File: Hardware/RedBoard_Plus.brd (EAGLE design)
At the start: 68.6 x 58.4 mm, 171 parts, among them IC3 LM1117, J2 ISP, J3 5.5x2.1mm Barrel, J4 QWIIC_RIGHT_ANGLE, J5 USB Female Type C Connector, Q1 20V/4.2A/52mΩ/1.4W, Q2 310mA/60V/1.6Ω, Q3 310mA/60V/1.6Ω, U3 3.3V, U4 ATMEGA328P_TQFP, U5 CH340C, Y1 16MHz

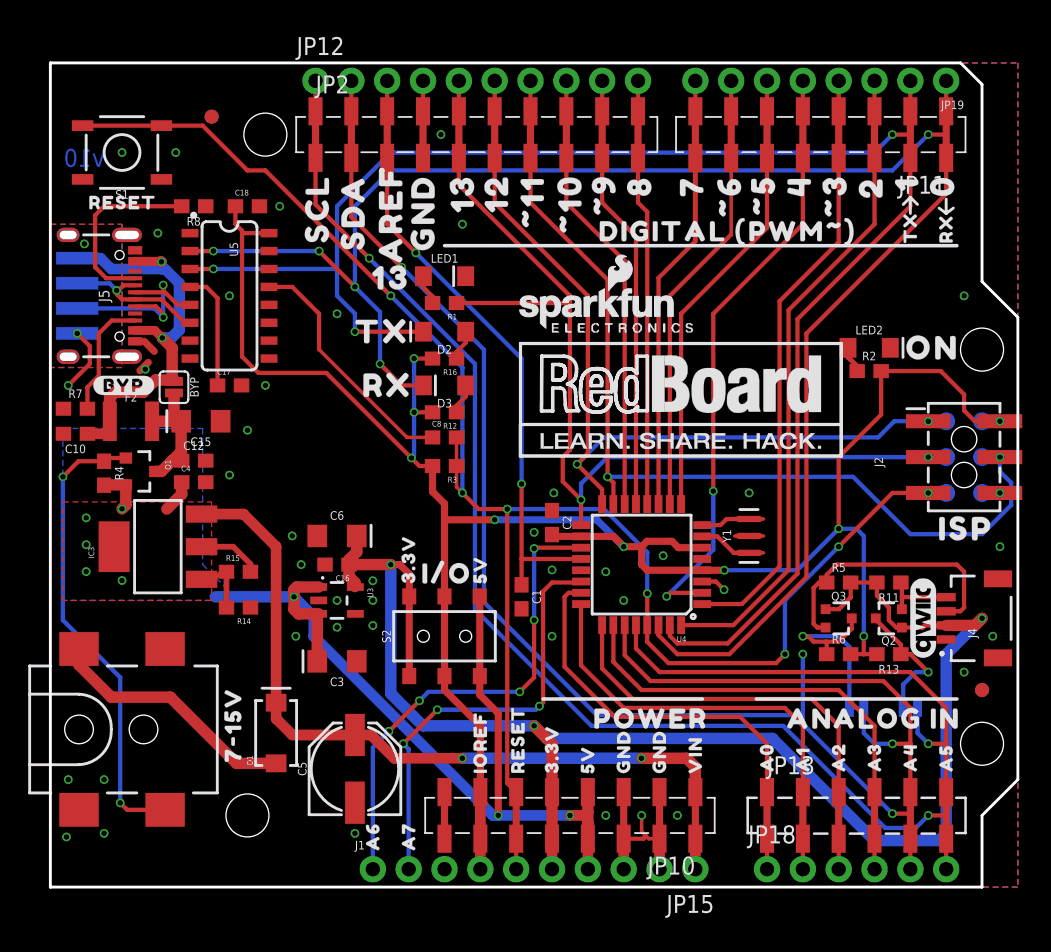
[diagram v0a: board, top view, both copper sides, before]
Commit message: Pete's design review notes:
SF logo on back
GND vias next to USB C
Remove 4-way nodes on sch
Remove overlapping text on sch
Move SFE logo in sch
Sch typo
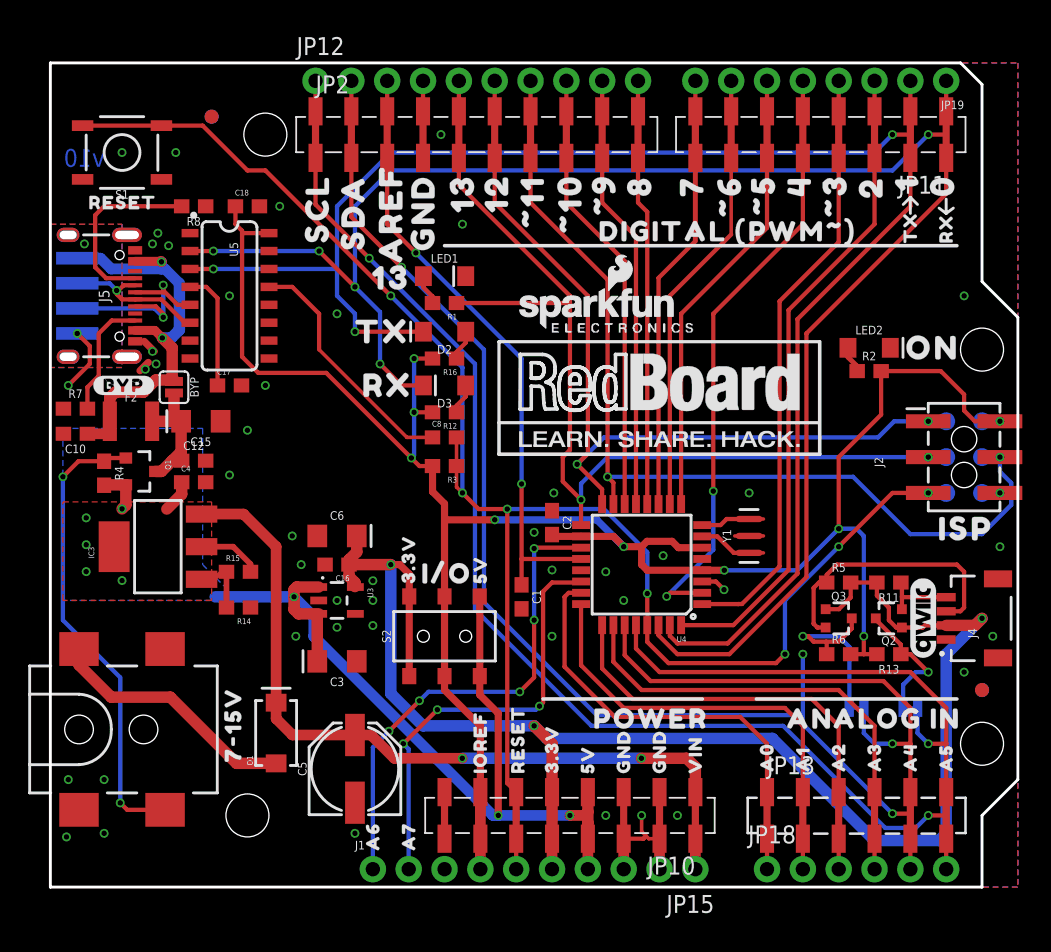
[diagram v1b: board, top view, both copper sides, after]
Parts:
- added U$101: (no value), SparkFun-Aesthetics:SFE_LOGO_FLAME_.2
- added U$3: REDBOARD_LOGO, redboard_logo:REDBOARD_LOGO
- U$78: value REDBOARD_LOGO -> (none); device redboard_logo:REDBOARD_LOGO -> SparkFun-Aesthetics:SFE_LOGO_NAME_.3
- moved U$1 33.5 mm to (31.8, 30.5), flipped to the top
- moved U$78 3.69 mm to (33.0, 26.7), flipped to the bottom
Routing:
- net GND: vias 44 -> 48
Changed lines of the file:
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@@
 <drawing>
 <settings>
-<setting alwaysvectorfont="no"/>
+<setting alwaysvectorfont="yes"/>
 <setting keepoldvectorfont="yes"/>
 <setting verticaltext="up"/>
@@
 <layers>
 <layer number="1" name="Top" color="4" fill="1" visible="yes" active="yes"/>
+<layer number="15" name="Route15" color="4" fill="6" visible="no" active="yes"/>
 <layer number="16" name="Bottom" color="1" fill="1" visible="yes" active="yes"/>
 <layer number="17" name="Pads" color="2" fill="1" visible="yes" active="yes"/>
@@
 <layer number="89" name="SimProbes" color="9" fill="1" visible="no" active="no"/>
 <layer number="90" name="Modules" color="5" fill="1" visible="no" active="no"/>
+<layer number="2" name="Route2" color="1" fill="3" visible="no" active="no"/>
 <layer number="3" name="Route3" color="4" fill="3" visible="no" active="no"/>
 <layer number="4" name="Route4" color="1" fill="4" visible="no" active="no"/>
@@
 <element name="U$100" library="output" package="_GND0" value="" x="26.416" y="43.307" smashed="yes" rot="R90"/>
 <element name="U$21" library="output" package="_GND0" value="" x="26.416" y="57.658" smashed="yes" rot="MR270"/>
-<element name="U$78" library="redboard_logo" package="REDBOARD_LOGO" value="REDBOARD_LOGO" x="33.274" y="30.353" smashed="yes"/>
-<element name="U$1" library="redboard_logo" package="REDBOARD_LOGO" value="REDBOARD_LOGO" x="62.992" y="42.672" smashed="yes" rot="MR0"/>
 <element name="FD1" library="SparkFun-Aesthetics" package="FIDUCIAL-1X2" value="FIDUCIAL1X2" x="11.43" y="54.61" smashed="yes" rot="MR0"/>
 <element name="FD2" library="SparkFun-Aesthetics" package="FIDUCIAL-1X2" value="FIDUCIAL1X2" x="66.04" y="13.97" smashed="yes" rot="MR0"/>
+<element name="U$1" library="redboard_logo" package="REDBOARD_LOGO" value="REDBOARD_LOGO" x="31.75" y="30.48" smashed="yes"/>
+<element name="U$3" library="redboard_logo" package="REDBOARD_LOGO" value="REDBOARD_LOGO" x="62.865" y="42.799" smashed="yes" rot="MR0"/>
+<element name="U$78" library="SparkFun-Aesthetics" package="SFE_LOGO_NAME_.3" value="" x="33.02" y="26.67" smashed="yes" rot="MR0"/>
+<element name="U$101" library="SparkFun-Aesthetics" package="SFE_LOGO_FLAME_.2" value="" x="29.21" y="31.75" smashed="yes" rot="MR0"/>
 </elements>
 <signals>
@@
 <wire x1="21.336" y1="54.99" x2="21.336" y2="51.69" width="0.254" layer="1"/>
 <contactref element="QW2" pad="1"/>
-<wire x1="57.658" y1="12.7" x2="57.658" y2="10.922" width="0.3048" layer="16"/>
+<wire x1="57.6707" y1="12.7" x2="57.658" y2="10.922" width="0.3048" layer="16"/>
 <wire x1="57.658" y1="10.922" x2="58.42" y2="10.16" width="0.3048" layer="16"/>
 <wire x1="58.42" y1="10.16" x2="59.69" y2="10.16" width="0.3048" layer="16"/>
@@
 <contactref element="QW1" pad="1"/>
 <wire x1="18.796" y1="54.61" x2="18.796" y2="51.69" width="0.254" layer="1"/>
-<wire x1="61.468" y1="12.7" x2="61.468" y2="10.922" width="0.3048" layer="16"/>
+<wire x1="61.4807" y1="12.7" x2="61.468" y2="10.922" width="0.3048" layer="16"/>
 <wire x1="61.468" y1="10.922" x2="62.23" y2="10.16" width="0.3048" layer="16"/>
 <via x="62.23" y="10.16" extent="1-16" drill="0.381"/>
@@
 <via x="1.27" y="35.56" extent="1-16" drill="0.381"/>
 <wire x1="2.794" y1="38.354" x2="2.794" y2="37.084" width="0.3048" layer="1"/>
+<via x="7.239" y="37.973" extent="1-16" drill="0.381"/>
+<via x="7.493" y="37.084" extent="1-16" drill="0.381"/>
+<via x="7.239" y="45.593" extent="1-16" drill="0.381"/>
+<via x="8.382" y="45.466" extent="1-16" drill="0.381"/>
 </signal>
 <signal name="AREF">
@@
 <wire x1="58.586" y1="18.884" x2="60.286" y2="17.184" width="0.3048" layer="1"/>
 <wire x1="60.286" y1="16.51" x2="60.286" y2="17.184" width="0.3048" layer="1"/>
-<wire x1="60.452" y1="12.7" x2="60.452" y2="14.351" width="0.3048" layer="16"/>
+<wire x1="60.4393" y1="12.7" x2="60.452" y2="14.351" width="0.3048" layer="16"/>
 <wire x1="61.341" y1="15.24" x2="62.23" y2="15.24" width="0.3048" layer="16"/>
 <wire x1="61.341" y1="15.24" x2="60.452" y2="14.351" width="0.3048" layer="16"/>
@@
 <contactref element="R6" pad="1"/>
 <contactref element="QW2" pad="2"/>
-<wire x1="56.642" y1="12.7" x2="56.642" y2="17.018" width="0.3048" layer="16"/>
+<wire x1="56.6293" y1="12.7" x2="56.642" y2="17.018" width="0.3048" layer="16"/>
 <wire x1="56.642" y1="17.018" x2="55.88" y2="17.78" width="0.3048" layer="16"/>
 <wire x1="55.88" y1="17.78" x2="53.34" y2="17.78" width="0.3048" layer="16"/>

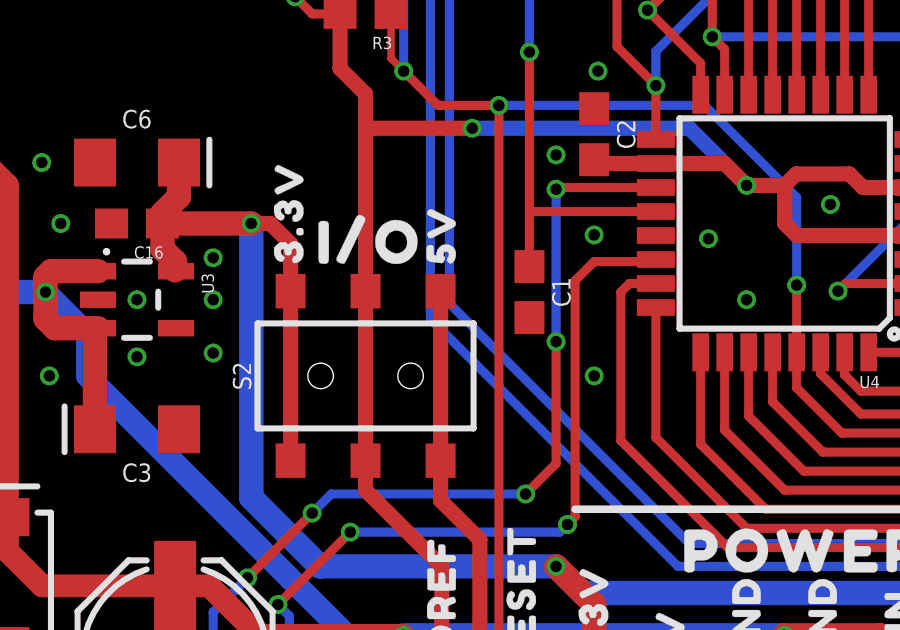
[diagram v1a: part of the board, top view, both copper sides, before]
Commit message: Design review changes
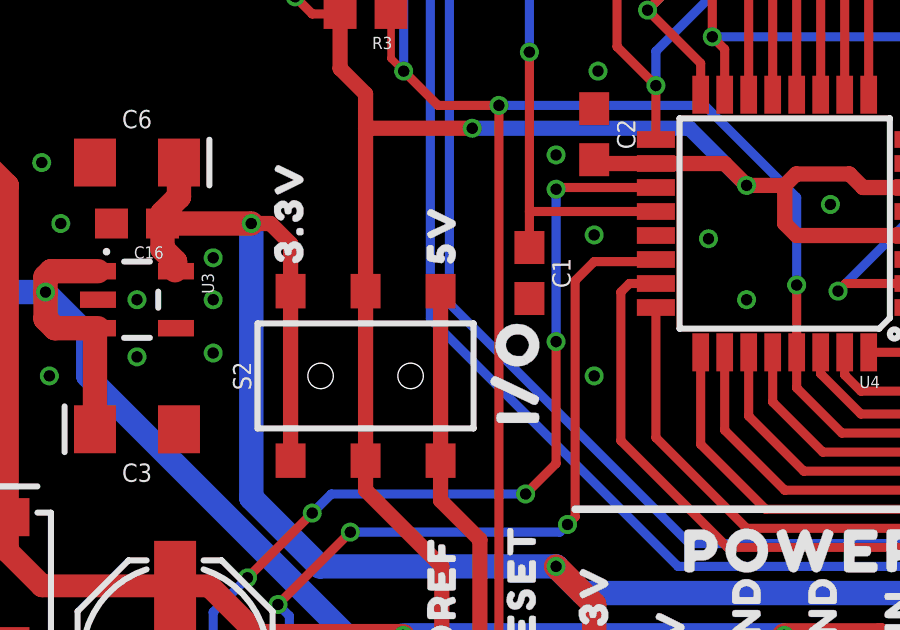
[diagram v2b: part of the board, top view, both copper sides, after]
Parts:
- moved U$42 10.5 mm to (33.0, 15.1), turned to 90 degrees
- moved C1 0.63 mm to (33.4, 21.2)
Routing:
- net AREF: track 43.9 -> 43.3 mm
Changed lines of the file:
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@@
 <layers>
 <layer number="1" name="Top" color="4" fill="1" visible="yes" active="yes"/>
-<layer number="15" name="Route15" color="4" fill="6" visible="no" active="yes"/>
 <layer number="16" name="Bottom" color="1" fill="1" visible="yes" active="yes"/>
 <layer number="17" name="Pads" color="2" fill="1" visible="yes" active="yes"/>
@@
 </autorouter>
 <elements>
-<element name="C1" library="SparkFun-Capacitors" package="0603" value="0.1uF" x="33.401" y="20.574" smashed="yes" rot="R270">
-<attribute name="NAME" x="34.163" y="20.574" size="0.6096" layer="25" font="vector" ratio="20" rot="R270" align="bottom-center"/>
-<attribute name="PROD_ID" value="CAP-00810" x="33.401" y="20.574" size="1.778" layer="27" rot="R270" display="off"/>
-<attribute name="VALUE" x="32.639" y="20.574" size="0.6096" layer="27" font="vector" ratio="15" rot="R270" align="top-center"/>
+<element name="C1" library="SparkFun-Capacitors" package="0603" value="0.1uF" x="33.401" y="21.209" smashed="yes" rot="R270">
+<attribute name="NAME" x="34.163" y="21.209" size="0.6096" layer="25" font="vector" ratio="20" rot="R270" align="bottom-center"/>
+<attribute name="PROD_ID" value="CAP-00810" x="33.401" y="21.209" size="1.778" layer="27" rot="R270" display="off"/>
+<attribute name="VALUE" x="32.639" y="21.209" size="0.6096" layer="27" font="vector" ratio="15" rot="R270" align="top-center"/>
 </element>
 <element name="R1" library="SparkFun-Resistors" package="0603" value="4.7k" x="27.94" y="41.402" smashed="yes" rot="R180">
@@
 <element name="U$43" library="output" package="3#3V0" value="" x="25.4" y="20.828" smashed="yes" rot="R90"/>
 <element name="U$44" library="output" package="5V0" value="" x="30.48" y="20.828" smashed="yes" rot="R90"/>
-<element name="U$42" library="output" package="I#O0" value="" x="25.273" y="22.225" smashed="yes"/>
+<element name="U$42" library="output" package="I#O0" value="" x="33.02" y="15.113" smashed="yes" rot="R90"/>
 <element name="U$45" library="output" package="ON0" value="" x="59.436" y="38.227" smashed="yes"/>
 <element name="U$46" library="output" package="ISP0" value="" x="61.722" y="25.4" smashed="yes"/>
@@
 <wire x1="33.401" y1="28.575" x2="33.401" y2="37.465" width="0.3048" layer="16"/>
 <contactref element="U4" pad="20"/>
-<wire x1="33.401" y1="21.424" x2="33.401" y2="23.26" width="0.3048" layer="1"/>
+<wire x1="33.401" y1="22.059" x2="33.401" y2="23.26" width="0.3048" layer="1"/>
 <wire x1="23.876" y1="51.69" x2="23.876" y2="46.99" width="0.3048" layer="1"/>
 <wire x1="23.876" y1="46.99" x2="25.908" y2="44.958" width="0.3048" layer="1"/>

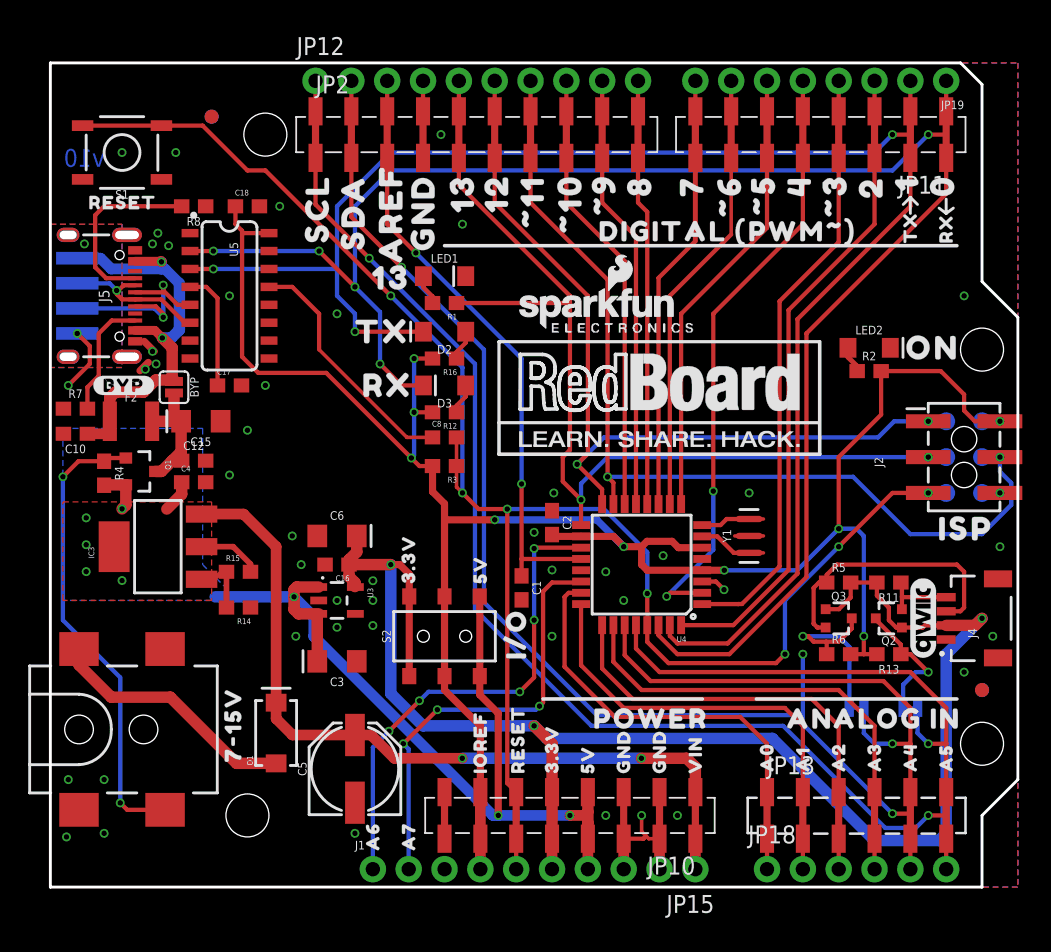
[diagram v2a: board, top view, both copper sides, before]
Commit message: Switch CH340C for CH340G with external oscillator
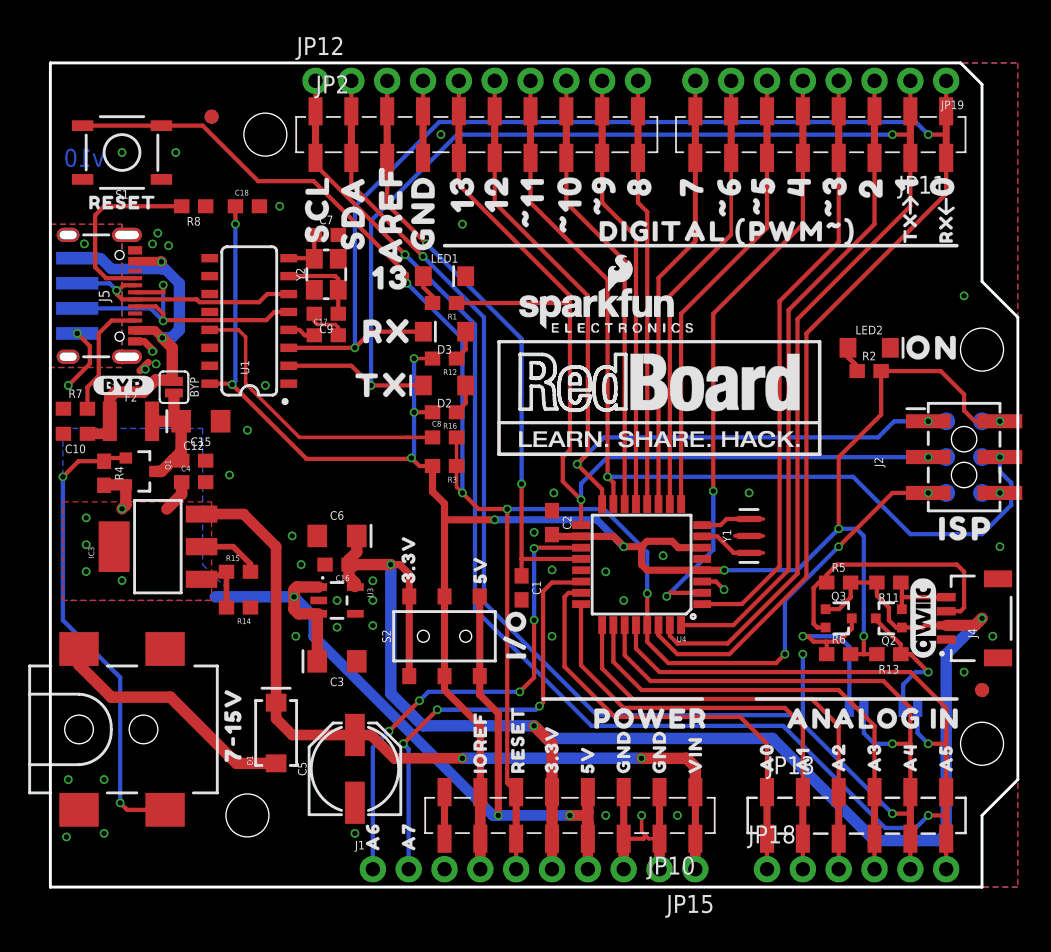
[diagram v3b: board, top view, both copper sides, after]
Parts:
- removed U5: CH340C, SparkFun-IC-Comms:SO016
- added C7, C9: 10pF, SparkFun-Capacitors:0603
- added U1: CH340G, SparkFun-IC-Comms:SO016
- added Y2: 12MHz, SparkFun-Clocks:CRYSTAL-SMD-3.2X2.5MM
- moved C17 7.73 mm to (19.6, 39.1)
- moved R12 3.81 mm to (27.9, 37.5)
- moved R16 3.81 mm to (27.9, 33.7)
- moved D2 3.81 mm to (27.9, 35.6)
- moved D3 3.81 mm to (27.9, 39.4)
- moved U$40 3.81 mm to (19.8, 35.6)
- moved U$41 3.81 mm to (20.3, 39.4)
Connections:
- net MISO renamed CIPO
- net MOSI renamed COPI
- removed net !DTR: C8.1, U5.13
- new net !DTR!: C8.1, U1.13
- new net N$10: C7.1, U1.8, Y2.3
- new net N$8: C9.1, U1.7, Y2.1
- net D+: now also U1.5; no longer U5.5
- net D-: now also U1.6; no longer U5.6
- net GND: now also C7.2, C9.2, U1.1, Y2.2, Y2.4; no longer U5.1
- net N$6: now also U1.4; no longer U5.4
- net RX-I: now also U1.3; no longer U5.2
- net TX-O: now also U1.2; no longer U5.3
- net VCC: now also U1.16; no longer U5.16
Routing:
- net !DTR!: track 0.00 -> 20.9 mm
- net !DTR: track 17.5 -> 0.00 mm
- net RX-I: track 126.9 -> 119.4 mm, vias 5 -> 2
- net D+: track 15.9 -> 23.4 mm
- net D-: track 10.8 -> 17.4 mm
- net N$6: track 8.47 -> 1.97 mm
- net N$8: track 0.00 -> 6.06 mm
- net TX-O: track 119.4 -> 114.5 mm, vias 3 -> 2
- net N$10: track 0.00 -> 3.52 mm
- net GND: track 19.2 -> 22.4 mm, vias 48 -> 46
- net !RESET: track 123.1 -> 124.6 mm
- net VCC: track 147.1 -> 148.7 mm, vias 9 -> 11
